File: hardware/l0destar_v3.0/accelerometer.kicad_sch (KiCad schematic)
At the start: 4 parts

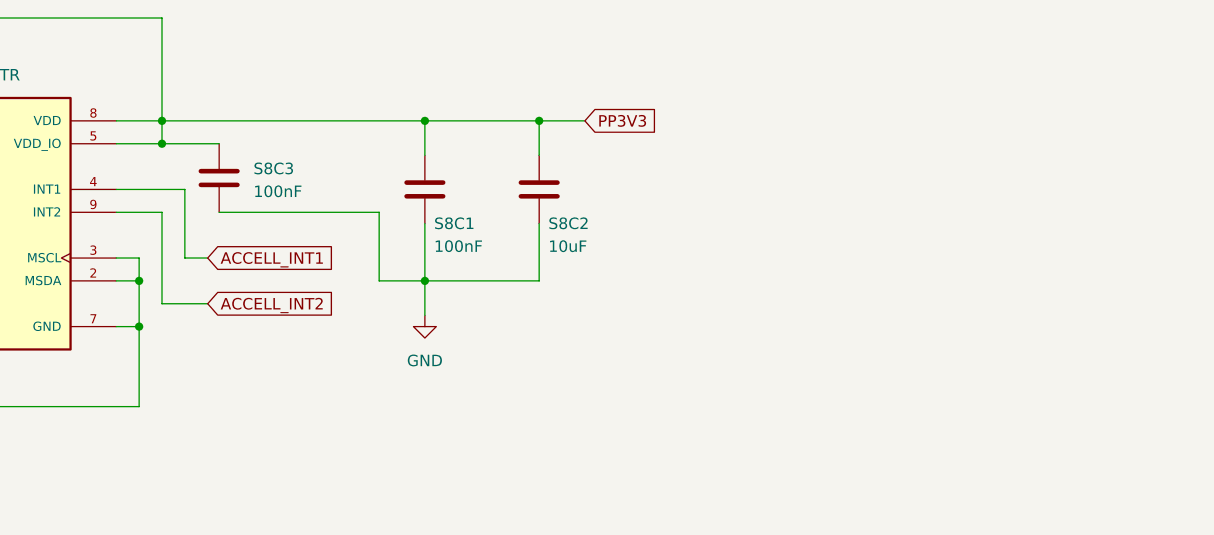
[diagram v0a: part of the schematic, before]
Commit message: updated v3.0 part specifications and added to the schematics
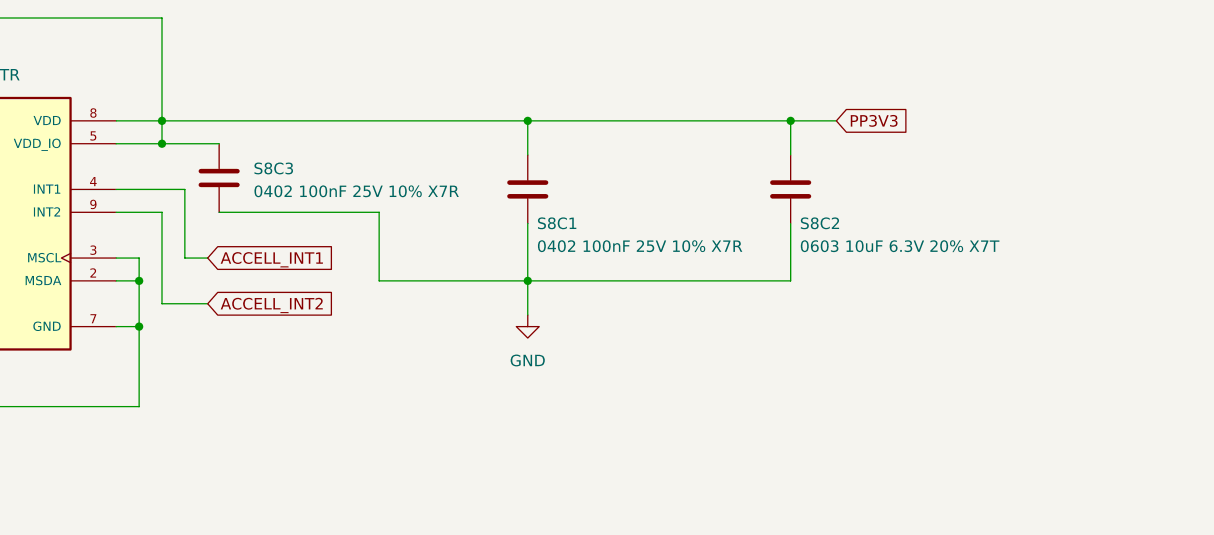
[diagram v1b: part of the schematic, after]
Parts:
- S8C1, S8C3: value 100nF -> 0402 100nF 25V 10% X7R
- S8C2: value 10uF -> 0603 10uF 6.3V 20% X7T
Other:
- moved on the sheet: S8C1, S8C2
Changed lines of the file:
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@@
 	)
 	(junction
-		(at 110.49 34.29)
-		(diameter 0)
-		(color 0 0 0 0)
-	)
-	(junction
-		(at 110.49 52.07)
+		(at 121.92 52.07)
 		(diameter 0)
 		(color 0 0 0 0)
@@
 	)
 	(junction
+		(at 121.92 34.29)
+		(diameter 0)
+		(color 0 0 0 0)
+	)
+	(junction
 		(at 81.28 34.29)
 		(diameter 0)
@@
 	)
 	(junction
-		(at 123.19 34.29)
+		(at 151.13 34.29)
 		(diameter 0)
 		(color 0 0 0 0)
@@
 	(wire
 		(pts
-			(xy 110.49 34.29) (xy 110.49 38.1)
+			(xy 121.92 34.29) (xy 121.92 38.1)
 		)
 		(stroke
@@
 	(wire
 		(pts
-			(xy 105.41 52.07) (xy 110.49 52.07)
+			(xy 105.41 52.07) (xy 121.92 52.07)
 		)
 		(stroke
@@
 	(wire
 		(pts
-			(xy 123.19 34.29) (xy 123.19 38.1)
+			(xy 151.13 34.29) (xy 151.13 38.1)
 		)
 		(stroke
@@
 	(wire
 		(pts
-			(xy 110.49 34.29) (xy 123.19 34.29)
+			(xy 121.92 34.29) (xy 151.13 34.29)
 		)
 		(stroke
@@
 	(wire
 		(pts
-			(xy 123.19 52.07) (xy 110.49 52.07)
+			(xy 151.13 52.07) (xy 121.92 52.07)
 		)
 		(stroke
@@
 	(wire
 		(pts
-			(xy 110.49 45.72) (xy 110.49 52.07)
+			(xy 121.92 45.72) (xy 121.92 52.07)
 		)
 		(stroke
@@
 	(wire
 		(pts
-			(xy 123.19 34.29) (xy 128.27 34.29)
+			(xy 151.13 34.29) (xy 156.21 34.29)
 		)
 		(stroke
@@
 	(wire
 		(pts
-			(xy 81.28 34.29) (xy 110.49 34.29)
+			(xy 81.28 34.29) (xy 121.92 34.29)
 		)
 		(stroke
@@
 	(wire
 		(pts
-			(xy 110.49 52.07) (xy 110.49 55.88)
+			(xy 121.92 52.07) (xy 121.92 55.88)
 		)
 		(stroke
@@
 	(wire
 		(pts
-			(xy 123.19 45.72) (xy 123.19 52.07)
+			(xy 151.13 45.72) (xy 151.13 52.07)
 		)
 		(stroke
@@
 	(global_label "PP3V3"
 		(shape input)
-		(at 128.27 34.29 0)
+		(at 156.21 34.29 0)
 		(fields_autoplaced yes)
 		(effects
@@
 		)
 		(property "Intersheetrefs" "${INTERSHEET_REFS}"
-			(at 137.3028 34.29 0)
+			(at 165.2428 34.29 0)
 			(hide yes)
 			(show_name no)
@@
 	(symbol
 		(lib_id "Device:C")
-		(at 123.19 41.91 0)
+		(at 151.13 41.91 0)
 		(unit 1)
 		(body_style 1)
@@
 		(dnp no)
 		(property "Reference" "S8C2"
-			(at 124.206 45.72 0)
+			(at 152.146 45.72 0)
 			(show_name no)
 			(do_not_autoplace no)
@@
 			)
 		)
-		(property "Value" "10uF"
-			(at 124.206 48.26 0)
+		(property "Value" "0603 10uF 6.3V 20% X7T"
+			(at 152.146 48.26 0)
 			(show_name no)
 			(do_not_autoplace no)
@@
 		)
 		(property "Footprint" "Capacitor_SMD:C_0603_1608Metric"
-			(at 124.1552 45.72 0)
+			(at 152.0952 45.72 0)
 			(hide yes)
 			(show_name no)
@@
 		)
 		(property "Datasheet" ""
-			(at 123.19 41.91 0)
+			(at 151.13 41.91 0)
 			(hide yes)
 			(show_name no)
@@
 		)
 		(property "Description" "Unpolarized capacitor"
-			(at 123.19 41.91 0)
+			(at 151.13 41.91 0)
 			(hide yes)
 			(show_name no)
@@
 	(symbol
 		(lib_id "Device:C")
-		(at 110.49 41.91 0)
+		(at 121.92 41.91 0)
 		(unit 1)
 		(body_style 1)
@@
 		(dnp no)
 		(property "Reference" "S8C1"
-			(at 111.506 45.72 0)
+			(at 122.936 45.72 0)
 			(show_name no)
 			(do_not_autoplace no)
@@
 			)
 		)
-		(property "Value" "100nF"
-			(at 111.506 48.26 0)
+		(property "Value" "0402 100nF 25V 10% X7R"
+			(at 122.936 48.26 0)
 			(show_name no)
 			(do_not_autoplace no)
@@
 		)
 		(property "Footprint" "Capacitor_SMD:C_0402_1005Metric"
-			(at 111.4552 45.72 0)
+			(at 122.8852 45.72 0)
 			(hide yes)
 			(show_name no)
@@
 		)
 		(property "Datasheet" ""
-			(at 110.49 41.91 0)
+			(at 121.92 41.91 0)
 			(hide yes)
 			(show_name no)
@@
 		)
 		(property "Description" "Unpolarized capacitor"
-			(at 110.49 41.91 0)
+			(at 121.92 41.91 0)
 			(hide yes)
 			(show_name no)
@@
 			)
 		)
-		(property "Value" "100nF"
+		(property "Value" "0402 100nF 25V 10% X7R"
 			(at 91.44 42.164 0)
 			(show_name no)
@@
 	(symbol
 		(lib_id "power:GND")
-		(at 110.49 55.88 0)
+		(at 121.92 55.88 0)
 		(unit 1)
 		(body_style 1)
@@
 		(fields_autoplaced yes)
 		(property "Reference" "#PWR059"
-			(at 110.49 62.23 0)
+			(at 121.92 62.23 0)
 			(hide yes)
 			(show_name no)
@@
 		)
 		(property "Value" "GND"
-			(at 110.49 60.96 0)
+			(at 121.92 60.96 0)
 			(show_name no)
 			(do_not_autoplace no)
@@
 		)
 		(property "Footprint" ""
-			(at 110.49 55.88 0)
+			(at 121.92 55.88 0)
 			(hide yes)
 			(show_name no)
@@
 		)
 		(property "Datasheet" ""
-			(at 110.49 55.88 0)
+			(at 121.92 55.88 0)
 			(hide yes)
 			(show_name no)
@@
 		)
 		(property "Description" "Power symbol creates a global label with name \"GND\" , ground"
-			(at 110.49 55.88 0)
-			(hide yes)
-			(show_name no)
+			(at 121.92 55.88 0)
+			(hide yes)
+			(show_name no)

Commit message: fix discrepencies
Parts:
- S8C1, S8C3: value 0402 100nF 25V 10% X7R -> 0402 100nF 10V 10% X7R
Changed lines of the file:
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@@
 			)
 		)
-		(property "Value" "0402 100nF 25V 10% X7R"
+		(property "Value" "0402 100nF 10V 10% X7R"
 			(at 122.936 48.26 0)
 			(show_name no)
@@
 			)
 		)
-		(property "Value" "0402 100nF 25V 10% X7R"
+		(property "Value" "0402 100nF 10V 10% X7R"
 			(at 91.44 42.164 0)
 			(show_name no)

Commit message: fix discrepencies
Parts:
- S8C2: value 0603 10uF 6.3V 20% X7T -> 0603 10uF 10V 20% X7T
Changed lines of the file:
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@@
 			)
 		)
-		(property "Value" "0603 10uF 6.3V 20% X7T"
+		(property "Value" "0603 10uF 10V 20% X7T"
 			(at 152.146 48.26 0)
 			(show_name no)
